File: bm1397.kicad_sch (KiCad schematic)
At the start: 0 parts

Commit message: moved over a lot of schematic from the bitaxe
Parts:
- added C18, C24, C26, C36, C37, C38, C39, C42, C43, C44, C45, C46, C47: 311-3342-1-ND, Capacitor_SMD:C_0402_1005Metric, symbol Device:C
- added C19, C20, C21, C22, C23, C25, C27, C28, C29, C31, C32, C33, C34, C35: 587-5514-1-ND, Capacitor_SMD:C_0402_1005Metric, symbol Device:C
- added C30: 330uF, Capacitor_Tantalum_SMD:CP_EIA-7343-31_Kemet-D_Pad2.25x2.55mm_HandSolder, symbol Device:C_Polarized
- added C40, C41: 1uF, Capacitor_SMD:C_0402_1005Metric, symbol Device:C
- added IC1: BM1397_mode1, bitaxe:BM1397, symbol bitaxe:BM1397_mode1
- added J3: Conn_01x05, Connector_PinHeader_2.54mm:PinHeader_1x05_P2.54mm_Vertical, symbol Connector_Generic:Conn_01x05
- added JP1, JP2: SolderJumper_2_Open, Jumper:SolderJumper-2_P1.3mm_Open_RoundedPad1.0x1.5mm, symbol Jumper:SolderJumper_2_Open
- added JP3: SolderJumper_2_Bridged, Jumper:SolderJumper-2_P1.3mm_Bridged2Bar_RoundedPad1.0x1.5mm, symbol Jumper:SolderJumper_2_Bridged
- added R13: 1k, Resistor_SMD:R_0402_1005Metric, symbol Device:R_US
- added R15, R16: 0, Resistor_SMD:R_0402_1005Metric, symbol Device:R_US
- added R17: 10k, Resistor_SMD:R_0402_1005Metric, symbol Device:R_US
- added TP10, TP11, TP12, TP13, TP14, TP15, TP16, TP17, TP18, TP3, TP4, TP5, TP6, TP7, TP8, TP9: TestPoint, TestPoint:TestPoint_Pad_D1.5mm, symbol Connector:TestPoint
- added U10, U5, U8, U9: SN74AXC1T45DBVR, bitaxe:SN74AXC1T45, symbol bitaxe:SN74AXC1T45DBVR
- added U4: 25MHz, bitaxe:O 25,0-JO32-B-1V3-1-T1-LF, symbol bitaxe:oscillator
- added U6: MCP1824T-1802E, Package_TO_SOT_SMD:SOT-23-5, symbol bitaxe:MCP1824
- added U7: MCP1824T-0802E, Package_TO_SOT_SMD:SOT-23-5, symbol bitaxe:MCP1824
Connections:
- new net: IC1.12 (CLKI), TP3.1, U4.3 (OUT)
- new net: IC1.29 (BO), TP9.1
- new net: IC1.5 (ADDR1), JP2.2 (B)
- new net: C19.2, C20.1, IC1.3 (VDD1_0)
- new net: IC1.25 (CLKO), TP12.1
- new net: C23.2, C25.1, IC1.1 (VDD3_0)
- new net: IC1.10 (RO), R15.2
- new net: IC1.11 (CI), R16.2
- new net: C20.2, C23.1, IC1.2 (VDD2_0)
- new net: IC1.20 (PIN_MODE), TP13.1
- new net: IC1.26 (CO), TP11.1
- new net: IC1.27 (RI), R17.1, TP14.1
- new net: IC1.28 (NRSTO), TP10.1
- new net: C34.2, C35.1, IC1.30 (VDD1_1)
- new net: C31.2, C34.1, IC1.31 (VDD2_1)
- new net: C29.2, C31.1, IC1.32 (VDD3_1)
- new net: IC1.4 (ADDR0), JP1.2 (B)
- new net: IC1.6 (ADDR2), JP3.2 (B)
- new net 0V8: C21.1, C33.1, C41.1, IC1.14 (PLL_VDD), IC1.15 (VDDIO_08_0), IC1.18 (VDDIO_08_1), TP18.1, U7.5 (VOUT)
- new net 1V8: C18.2, C22.1, C32.1, C36.1, C40.1, C42.1, C44.1, C46.1, IC1.16 (VDDIO_18_0), IC1.17 (VDDIO_18_1), J3.1 (Pin_1), R17.2, TP17.1, U10.1 (VCCA), U4.1 (EN), U4.4 (VIN), U5.1 (VCCA), U6.5 (VOUT), U8.1 (VCCA), U9.1 (VCCA)
- new net 3V3: C37.1, C43.1, C45.1, C47.1, U10.6 (VCCB), U5.6 (VCCB), U8.6 (VCCB), U9.6 (VCCB)
- new net 5V: C38.1, C39.1, U6.1 (VIN), U6.3 (EN), U7.1 (VIN), U7.3 (EN)
- new net BM_BI: IC1.8 (BI), TP8.1
- new net CI: J3.2 (Pin_2), R16.1, TP4.1
- new net GND: C18.1, C19.1, C21.2, C22.2, C24.2, C26.2, C27.2, C28.2, C30.2, C32.2, C33.2, C35.2, C36.2, C37.2, C38.2, C39.2, C40.2, C41.2, C42.2, C43.2, C44.2, C45.2, C46.2, C47.2, IC1.13 (PLL_VSS), IC1.19 (VSS), IC1.34 (VSS_0), J3.5 (Pin_5), JP1.1 (A), JP2.1 (A), JP3.1 (A), R13.1, TP7.1, U10.2 (GND), U10.5 (DIR), U4.2 (GND), U5.2 (GND), U5.5 (DIR), U6.2 (GND), U7.2 (GND), U8.2 (GND), U8.5 (DIR), U9.2 (GND), U9.5 (DIR)
- new net RO: J3.3 (Pin_3), R15.1, TP5.1
- new net RST_N: IC1.9 (NRSTI), J3.4 (Pin_4), R13.2, TP6.1
- new net TEMP_N: IC1.21 (TEMP_N), TP16.1
- new net TEMP_P: IC1.22 (TEMP_P), TP15.1
- new net VDD: C24.1, C25.2, C26.1, C27.1, C28.1, C29.1, C30.1, IC1.33 (VDD)
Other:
- note added: "DIR LOW is B -> A"
- note added: "Reference Voltage Regulators"

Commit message: more schematic
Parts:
- removed R15, R16: 0, Resistor_SMD:R_0402_1005Metric, symbol Device:R_US
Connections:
- net 1V8: now also U8.5 (DIR)
- net BM_BI: now also U10.3 (A)
- net CI: now also U9.4 (B)
- net GND: no longer U8.5 (DIR)
- net RO: now also U8.4 (B)
- net RST_N: no longer IC1.9 (NRSTI), R13.2
- net BM_RST_N: now reaches U5.3 (A)
- net BM_RST_N: now also IC1.9 (NRSTI), R13.2
- net RST: now reaches U5.4 (B)
- net BM_RO: now reaches IC1.10 (RO)
- net BM_RO: now also U8.3 (A)
- net BM_CI: now reaches IC1.11 (CI)
- net BM_CI: now also U9.3 (A)
- net BI: now reaches U10.4 (B)
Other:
- note added: "DIR HI is A -> B"
- note added: "DIR LOW is A <- B"
- note removed: "DIR LOW is B -> A"

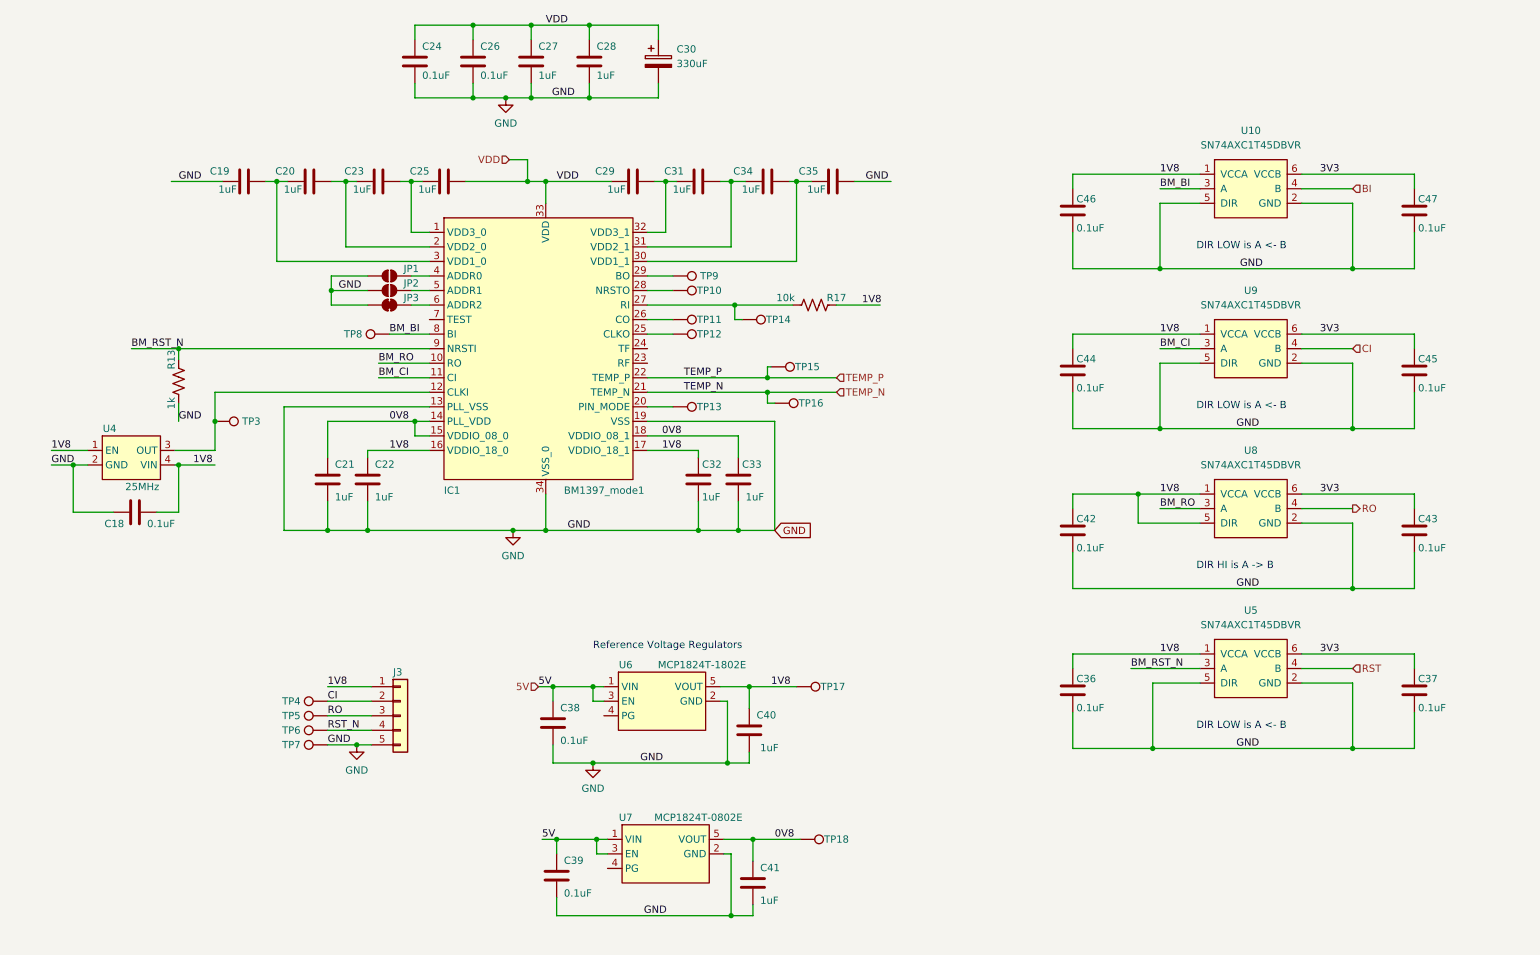
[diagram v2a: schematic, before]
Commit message: cleared up some part reference designator madness
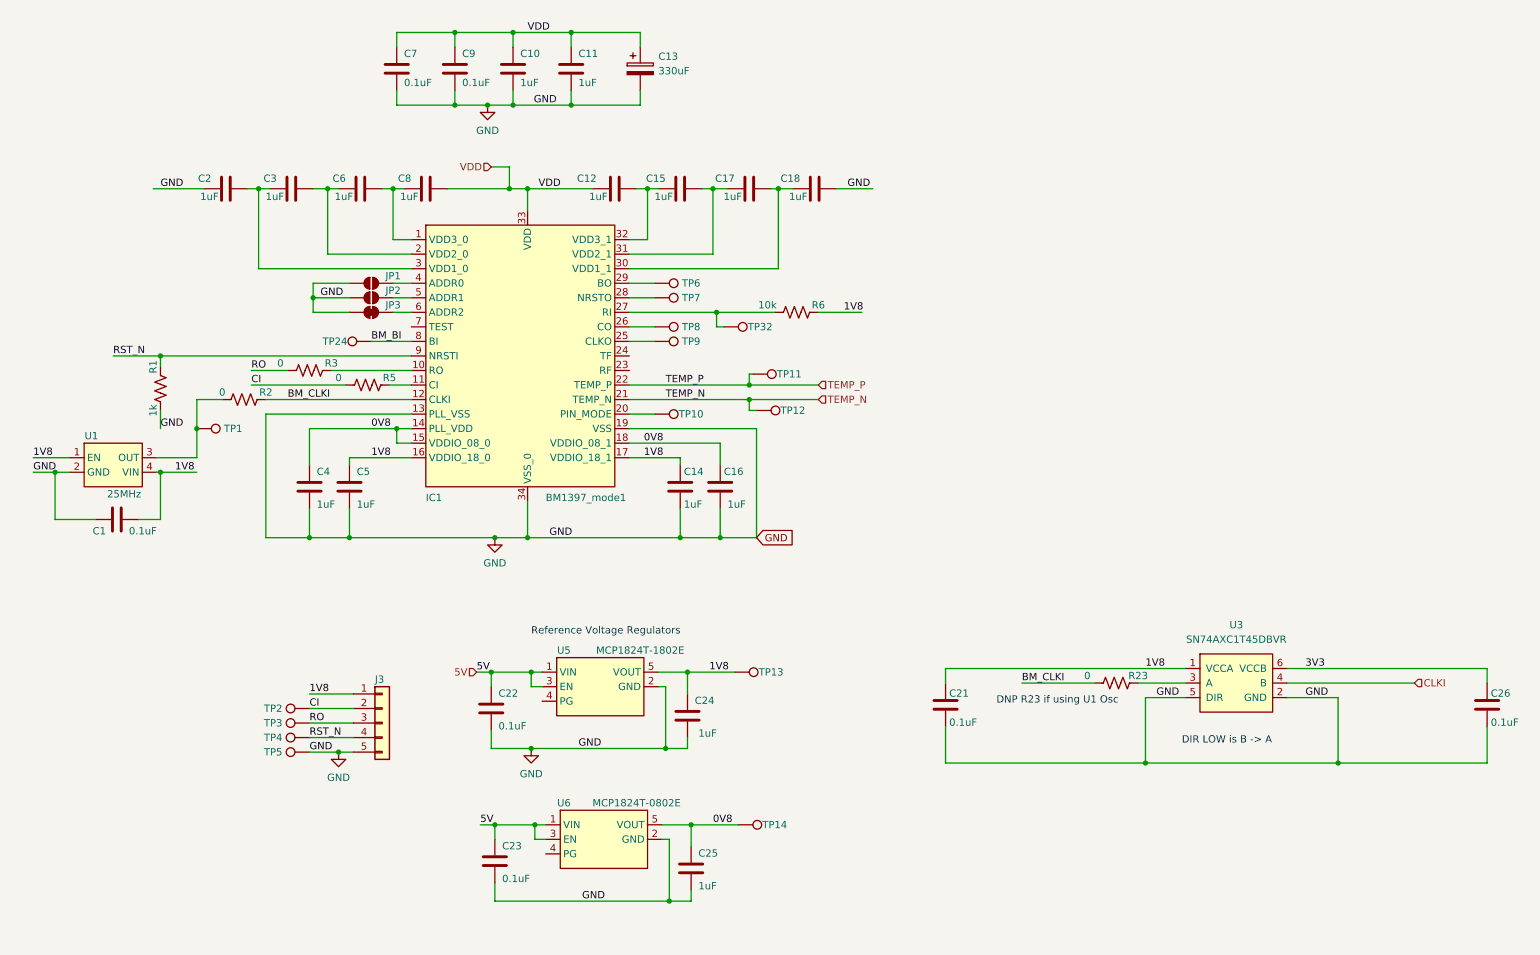
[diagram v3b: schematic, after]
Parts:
- removed C19, C20, C27, C28, C29, C31, C32, C33, C34, C35: 587-5514-1-ND, Capacitor_SMD:C_0402_1005Metric, symbol Device:C
- removed C30: 330uF, Capacitor_Tantalum_SMD:CP_EIA-7343-31_Kemet-D_Pad2.25x2.55mm_HandSolder, symbol Device:C_Polarized
- removed C36, C37, C38, C39, C42, C43, C44, C45, C46, C47: 311-3342-1-ND, Capacitor_SMD:C_0402_1005Metric, symbol Device:C
- removed C40, C41: 1uF, Capacitor_SMD:C_0402_1005Metric, symbol Device:C
- removed R13: 1k, Resistor_SMD:R_0402_1005Metric, symbol Device:R_US
- removed R17: 10k, Resistor_SMD:R_0402_1005Metric, symbol Device:R_US
- removed TP15, TP16, TP17, TP18: TestPoint, TestPoint:TestPoint_Pad_D1.5mm, symbol Connector:TestPoint
- removed U10, U5, U8, U9: SN74AXC1T45DBVR, bitaxe:SN74AXC1T45, symbol bitaxe:SN74AXC1T45DBVR
- removed U4: 25MHz, bitaxe:O 25,0-JO32-B-1V3-1-T1-LF, symbol bitaxe:oscillator
- removed U7: MCP1824T-0802E, Package_TO_SOT_SMD:SOT-23-5, symbol bitaxe:MCP1824
- added C1, C7, C9: 311-3342-1-ND, Capacitor_SMD:C_0402_1005Metric, symbol Device:C
- added C10, C11, C12, C14, C15, C16, C17, C2, C3, C4, C5, C6, C8: 587-5514-1-ND, Capacitor_SMD:C_0402_1005Metric, symbol Device:C
- added C13: 330uF, Capacitor_Tantalum_SMD:CP_EIA-7343-31_Kemet-D_Pad2.25x2.55mm_HandSolder, symbol Device:C_Polarized
- added R1: 1k, Resistor_SMD:R_0402_1005Metric, symbol Device:R_US
- added R2, R23, R3, R5: 0, Resistor_SMD:R_0402_1005Metric, symbol Device:R_US
- added R6: 10k, Resistor_SMD:R_0402_1005Metric, symbol Device:R_US
- added TP1, TP2, TP24, TP32: TestPoint, TestPoint:TestPoint_Pad_D1.5mm, symbol Connector:TestPoint
- added U1: 25MHz, bitaxe:O 25,0-JO32-B-1V3-1-T1-LF, symbol bitaxe:oscillator
- added U3: SN74AXC1T45DBVR, bitaxe:SN74AXC1T45, symbol bitaxe:SN74AXC1T45DBVR
- added U5: MCP1824T-1802E, Package_TO_SOT_SMD:SOT-23-5, symbol bitaxe:MCP1824
- C18: value 311-3342-1-ND -> 587-5514-1-ND; DK 1292-1639-1-ND -> 587-5514-1-ND; PARTNO 0402X104K100CT -> EMK105BJ105MV-F
- C21, C22, C23: value 587-5514-1-ND -> 311-3342-1-ND; DK 587-5514-1-ND -> 1292-1639-1-ND; PARTNO EMK105BJ105MV-F -> 0402X104K100CT
- C24: value 311-3342-1-ND -> 1uF; DK 1292-1639-1-ND -> 587-5514-1-ND; PARTNO 0402X104K100CT -> EMK105BJ105MV-F
- C25: value 587-5514-1-ND -> 1uF
- U6: value MCP1824T-1802E -> MCP1824T-0802E; DK MCP1824T-1802E/OTCT-ND -> MCP1824T-0802E/OTCT-ND; PARTNO MCP1824T-1802E/OT -> MCP1824T-0802E/OT
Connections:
- net BM_RST_N is gone; now on net RST_N: IC1.9 (NRSTI)
- net 0V8: now also C25.1, TP14.1, U6.5 (VOUT), C16.1, C4.1; no longer C21.1
- net 1V8: now also C21.1, C24.1, TP13.1, C1.2, C14.1, C5.1, R6.2, U1.1 (EN), U1.4 (VIN), U3.1 (VCCA), U5.5 (VOUT); no longer C18.2, C22.1, U6.5 (VOUT)
- net 3V3: now also C26.1, U3.6 (VCCB)
- net 5V: now also C22.1, C23.1, U5.1 (VIN), U5.3 (EN)
- net BM_BI: now also TP24.1; no longer TP8.1
- net CI: now also R5.1, TP2.1; no longer TP4.1
- net GND: now also C18.2, C23.2, C25.2, TP5.1, C1.1, C10.2, C11.2, C13.2, C14.2, C16.2, C2.1, C4.2, C5.2, C7.2, C9.2, R1.1, U1.2 (GND), U3.2 (GND), U3.5 (DIR), U5.2 (GND); no longer C18.1, TP7.1
- net RO: now also TP3.1, R3.1; no longer TP5.1
- net RST_N: now also TP4.1, R1.2; no longer TP6.1
- net TEMP_N: now also TP12.1
- net TEMP_P: now also TP11.1
- net VDD: now also C10.1, C11.1, C12.1, C13.1, C7.1, C8.2, C9.1; no longer C24.1, C25.2, C26.1
- net BM_CLKI: now reaches IC1.12 (CLKI)
- net BM_CLKI: now also R2.2, R23.1; no longer TP3.1
- net at TP9.1: now also IC1.25 (CLKO); no longer IC1.29 (BO)
- net at IC1.3 (VDD1_0): now also C2.2, C3.1
- net at IC1.2 (VDD2_0): now also C3.2, C6.1; no longer C23.1
- net at IC1.20 (PIN_MODE): now also TP10.1; no longer TP13.1
- net at IC1.26 (CO): now also TP8.1; no longer TP11.1
- net at IC1.27 (RI): now also R6.1, TP32.1; no longer TP14.1
- net at IC1.28 (NRSTO): now also TP7.1; no longer TP10.1
- net at IC1.30 (VDD1_1): now also C18.1, C17.2
- net at IC1.31 (VDD2_1): now also C15.2, C17.1
- net at IC1.32 (VDD3_1): now also C12.2, C15.1
- net BM_CI: no longer names the net of IC1.11 (CI)
- net BM_CI: now also R5.2
- net BM_RO: no longer names the net of IC1.10 (RO)
- net BM_RO: now also R3.2
- new net: R23.2, U3.3 (A)
- new net: C6.2, C8.1, IC1.1 (VDD3_0)
- new net: IC1.29 (BO), TP6.1
- new net: R2.1, TP1.1, U1.3 (OUT)
- new net CLKI: U3.4 (B)
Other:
- note added: "DIR LOW is B -> A"
- note added: "DNP R23 if using U1 Osc"
- note removed: "DIR HI is A -> B"
- note removed: "DIR LOW is A <- B"

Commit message: swapped out the VCCIO LDOs for some LCSC versions
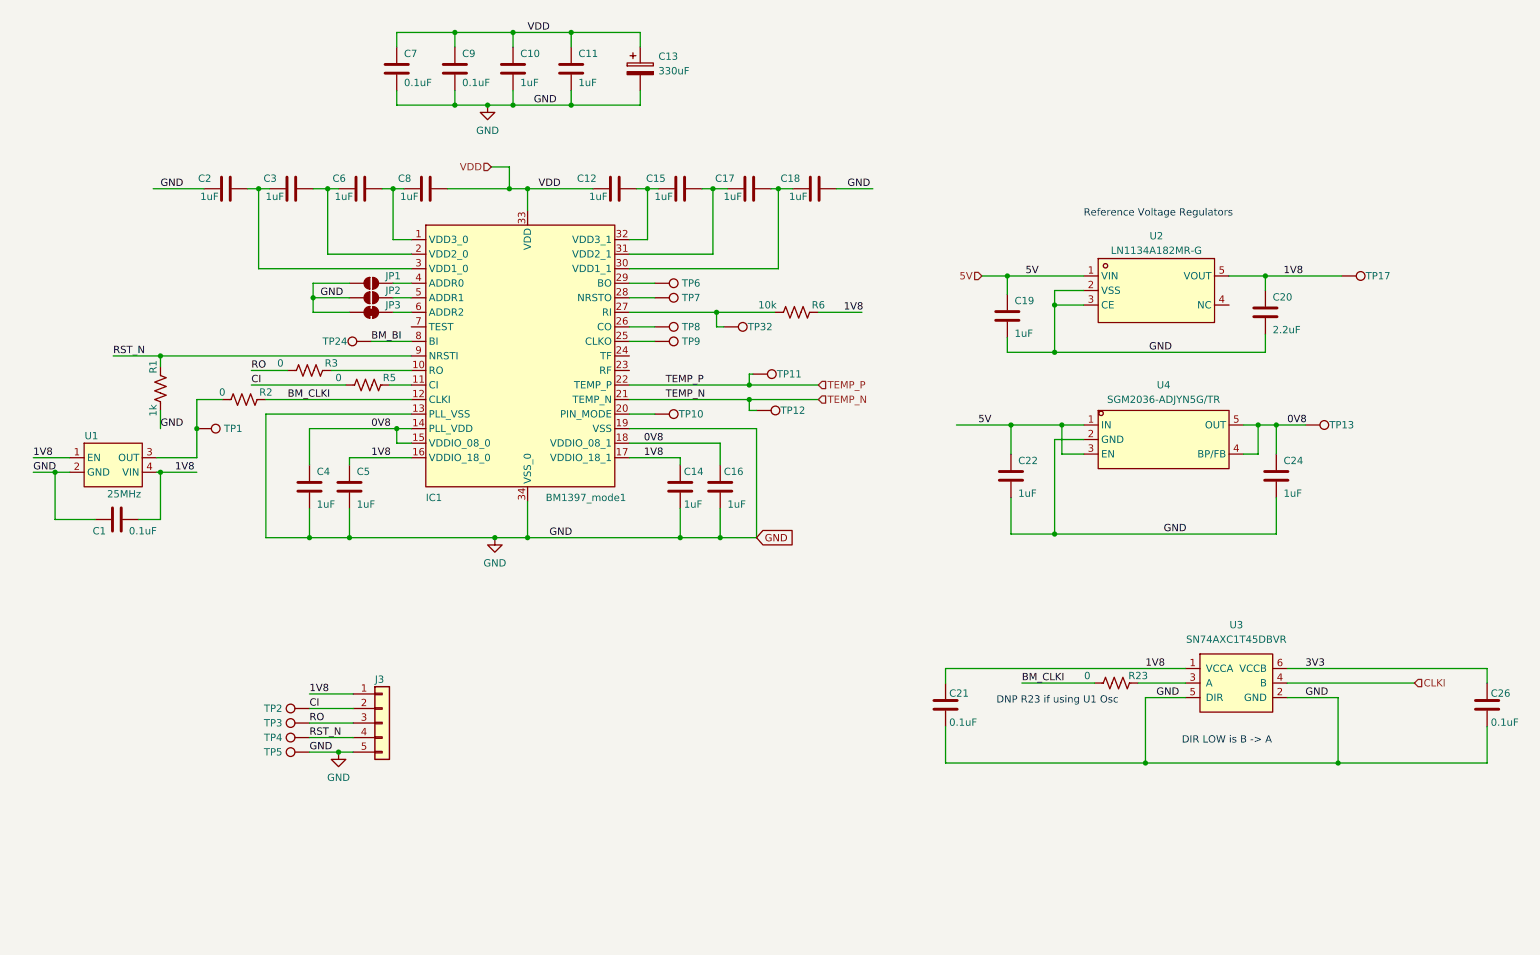
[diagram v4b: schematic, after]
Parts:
- removed C23: 311-3342-1-ND, Capacitor_SMD:C_0402_1005Metric, symbol Device:C
- removed C25: 1uF, Capacitor_SMD:C_0402_1005Metric, symbol Device:C
- removed TP14: TestPoint, TestPoint:TestPoint_Pad_D1.5mm, symbol Connector:TestPoint
- removed U5: MCP1824T-1802E, Package_TO_SOT_SMD:SOT-23-5, symbol bitaxe:MCP1824
- removed U6: MCP1824T-0802E, Package_TO_SOT_SMD:SOT-23-5, symbol bitaxe:MCP1824
- added C19: 1uF, Capacitor_SMD:C_0402_1005Metric, symbol Device:C
- added C20: 2.2uF, Capacitor_SMD:C_0402_1005Metric, symbol Device:C
- added TP17: TestPoint, TestPoint:TestPoint_Pad_D1.5mm, symbol Connector:TestPoint
- added U2: LN1134A182MR-G, lcsc:SOT-23-5_L3.0-W1.7-P0.95-LS2.8-BR, symbol lcsc:LN1134A182MR-G
- added U4: SGM2036-ADJYN5G/TR, lcsc:SOT-23-5_L3.0-W1.7-P0.95-LS2.8-BR, symbol lcsc:SGM2036-ADJYN5G_TR
- C22: value 311-3342-1-ND -> 1uF; DK 1292-1639-1-ND -> (none); PARTNO 0402X104K100CT -> (none)
- C24: DK 587-5514-1-ND -> (none); PARTNO EMK105BJ105MV-F -> (none)
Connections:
- net 0V8: now also C24.1, TP13.1, U4.4 (BP/FB), U4.5 (OUT)
- net 1V8: now also C20.1, TP17.1, U2.5 (VOUT); no longer C24.1, TP13.1
- net 5V: now also C19.1, U2.1 (VIN), U4.1 (IN), U4.3 (EN)
- net GND: now also C19.2, C20.2, U2.2 (VSS), U2.3 (CE), U4.2 (GND)
